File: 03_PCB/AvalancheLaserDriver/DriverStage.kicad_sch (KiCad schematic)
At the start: 20 parts

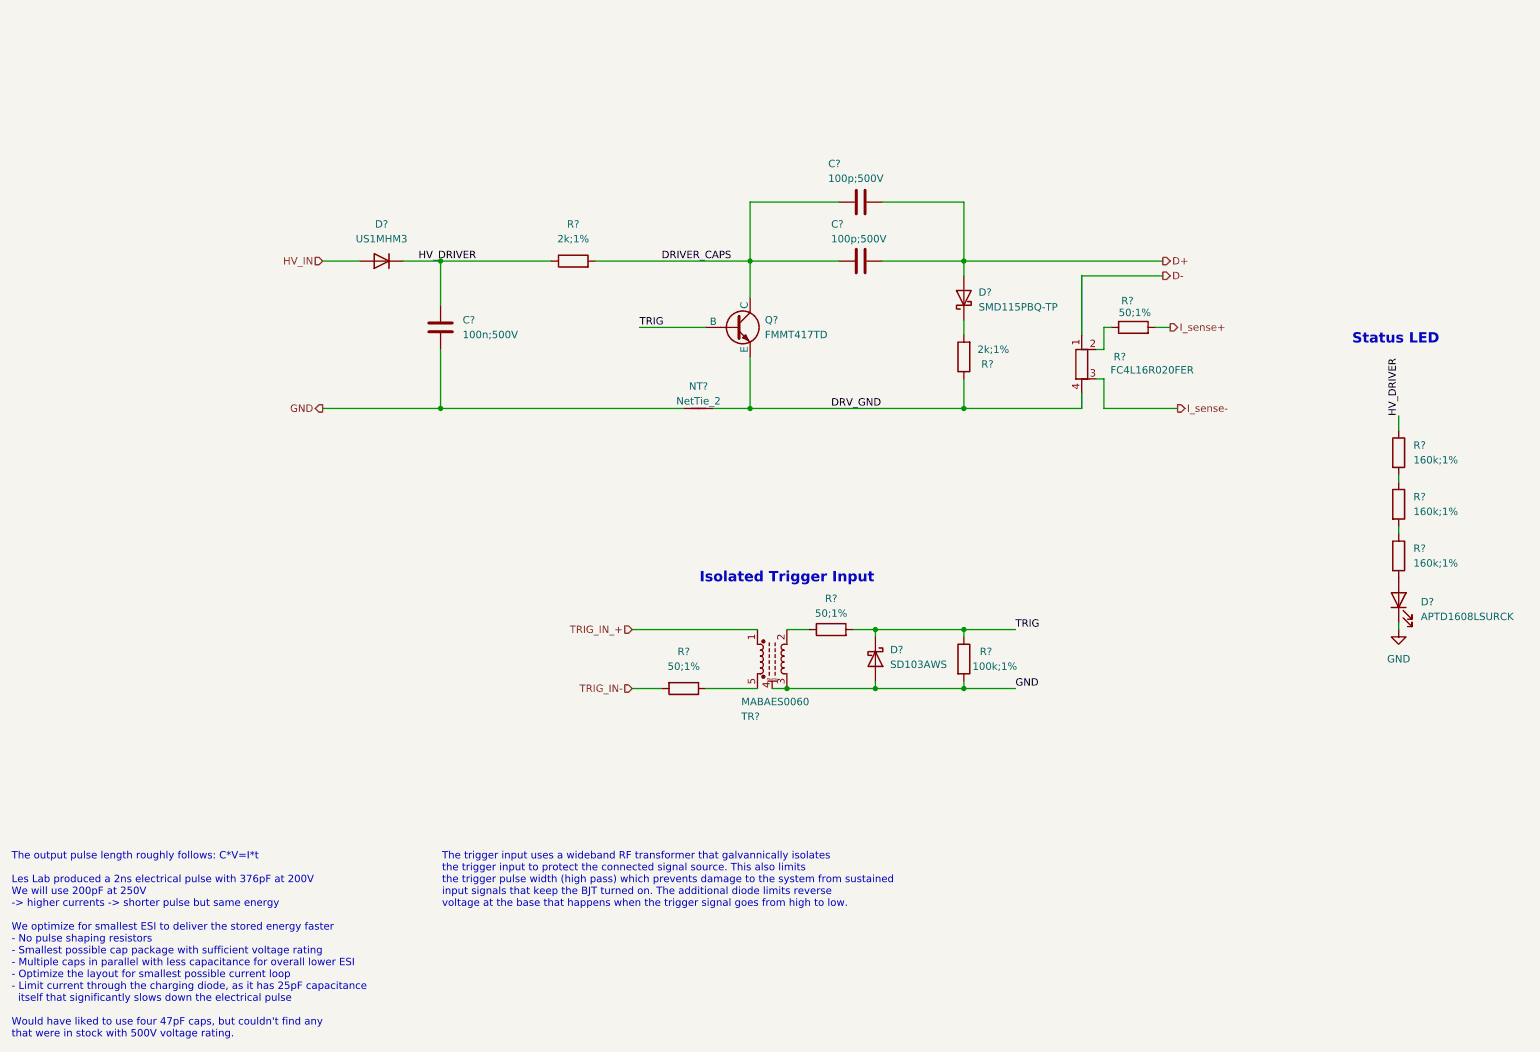
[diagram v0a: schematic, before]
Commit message: feat(pcb): edit component values after assembling first prototype
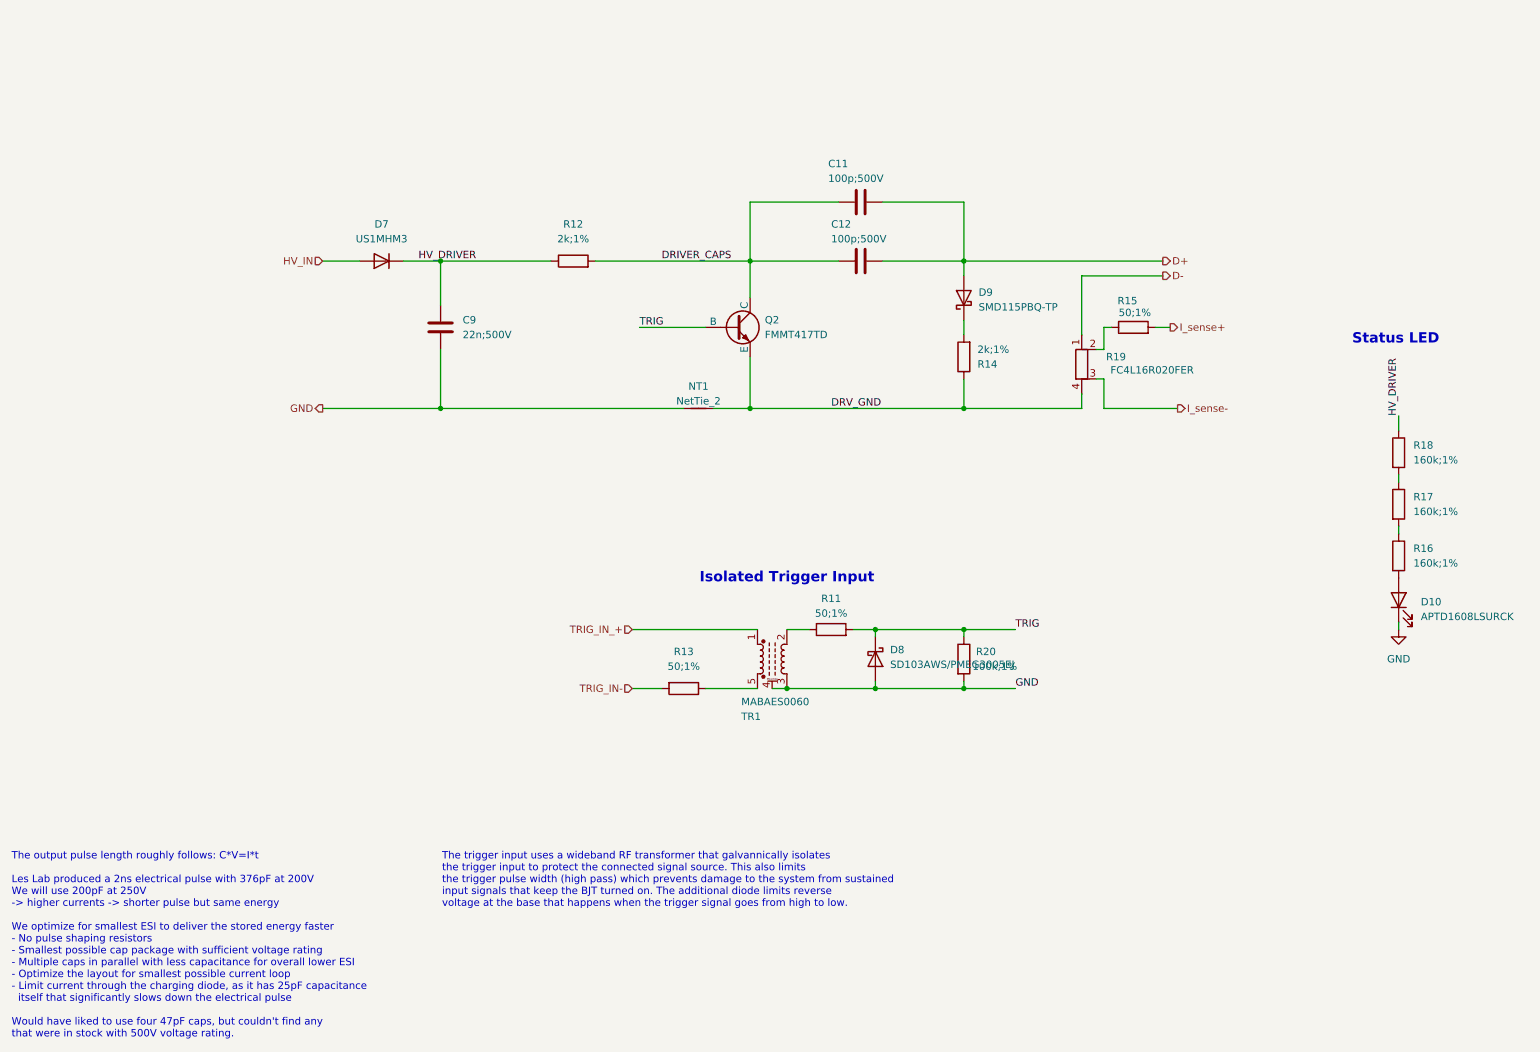
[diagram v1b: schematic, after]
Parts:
- C9: renamed from C?; value 100n;500V -> 22n;500V
- D8: renamed from D?; value SD103AWS -> SD103AWS/PMEG3005EJ
- gave numbers to parts that had none: 18
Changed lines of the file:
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@@
 		(dnp no)
 		(fields_autoplaced yes)
-		(property "Reference" "D?"
+		(property "Reference" "D7"
 			(at 78.74 57.15 0)
 			(effects
@@
 		(dnp no)
 		(fields_autoplaced yes)
-		(property "Reference" "R?"
+		(property "Reference" "R18"
 			(at 256.54 95.2499 0)
 			(effects
@@
 		(on_board yes)
 		(dnp no)
-		(property "Reference" "R?"
+		(property "Reference" "R20"
 			(at 182.88 130.81 0)
 			(effects
@@
 		(dnp no)
 		(fields_autoplaced yes)
-		(property "Reference" "D?"
+		(property "Reference" "D10"
 			(at 257.81 122.2374 90)
 			(effects
@@
 		(dnp no)
 		(fields_autoplaced yes)
-		(property "Reference" "#PWR?"
+		(property "Reference" "#PWR07"
 			(at 254 133.35 0)
 			(effects
@@
 		(dnp no)
 		(fields_autoplaced yes)
-		(property "Reference" "R?"
+		(property "Reference" "R16"
 			(at 256.54 113.0299 0)
 			(effects
@@
 		(dnp no)
 		(fields_autoplaced yes)
-		(property "Reference" "D?"
+		(property "Reference" "D9"
 			(at 181.61 68.8974 90)
 			(effects
@@
 		(on_board yes)
 		(dnp no)
-		(property "Reference" "TR?"
+		(property "Reference" "TR1"
 			(at 140.716 141.986 90)
 			(effects
@@
 		(on_board yes)
 		(dnp no)
-		(property "Reference" "R?"
+		(property "Reference" "R12"
 			(at 111.76 57.15 90)
 			(effects
@@
 		(dnp no)
 		(fields_autoplaced yes)
-		(property "Reference" "D?"
+		(property "Reference" "D8"
 			(at 166.37 130.4924 90)
 			(effects
@@
 			)
 		)
-		(property "Value" "SD103AWS"
+		(property "Value" "SD103AWS/PMEG3005EJ"
 			(at 166.37 133.0324 90)
 			(effects
@@
 		(on_board yes)
 		(dnp no)
-		(property "Reference" "C?"
+		(property "Reference" "C12"
 			(at 156.21 57.15 90)
 			(effects
@@
 		(on_board yes)
 		(dnp no)
-		(property "Reference" "NT?"
+		(property "Reference" "NT1"
 			(at 133.35 85.09 0)
 			(effects
@@
 		(dnp no)
 		(fields_autoplaced yes)
-		(property "Reference" "R?"
+		(property "Reference" "R17"
 			(at 256.54 104.1399 0)
 			(effects
@@
 		(on_board yes)
 		(dnp no)
-		(property "Reference" "R?"
+		(property "Reference" "R15"
 			(at 207.264 70.358 90)
 			(effects
@@
 		(dnp no)
 		(fields_autoplaced yes)
-		(property "Reference" "C?"
+		(property "Reference" "C9"
 			(at 92.71 73.6599 0)
 			(effects
@@
 			)
 		)
-		(property "Value" "100n;500V"
+		(property "Value" "22n;500V"
 			(at 92.71 76.1999 0)
 			(effects
@@
 		(on_board yes)
 		(dnp no)
-		(property "Reference" "R?"
+		(property "Reference" "R14"
 			(at 183.134 81.28 0)
 			(effects
@@
 		(on_board yes)
 		(dnp no)
-		(property "Reference" "Q?"
+		(property "Reference" "Q2"
 			(at 144.78 73.6599 0)
 			(effects
@@
 		(on_board yes)
 		(dnp no)
-		(property "Reference" "R?"
+		(property "Reference" "R11"
 			(at 156.21 121.666 90)
 			(effects
@@
 		(dnp no)
 		(fields_autoplaced yes)
-		(property "Reference" "R?"
+		(property "Reference" "R13"
 			(at 130.81 130.81 90)
 			(effects
@@
 		(on_board yes)
 		(dnp no)
-		(property "Reference" "R?"
+		(property "Reference" "R19"
 			(at 207.01 80.01 0)
 			(effects
@@
 		(on_board yes)
 		(dnp no)
-		(property "Reference" "C?"
+		(property "Reference" "C11"
 			(at 155.702 46.736 90)
 			(effects

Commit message: feat(pcb): update laser driver circuit after first iteration
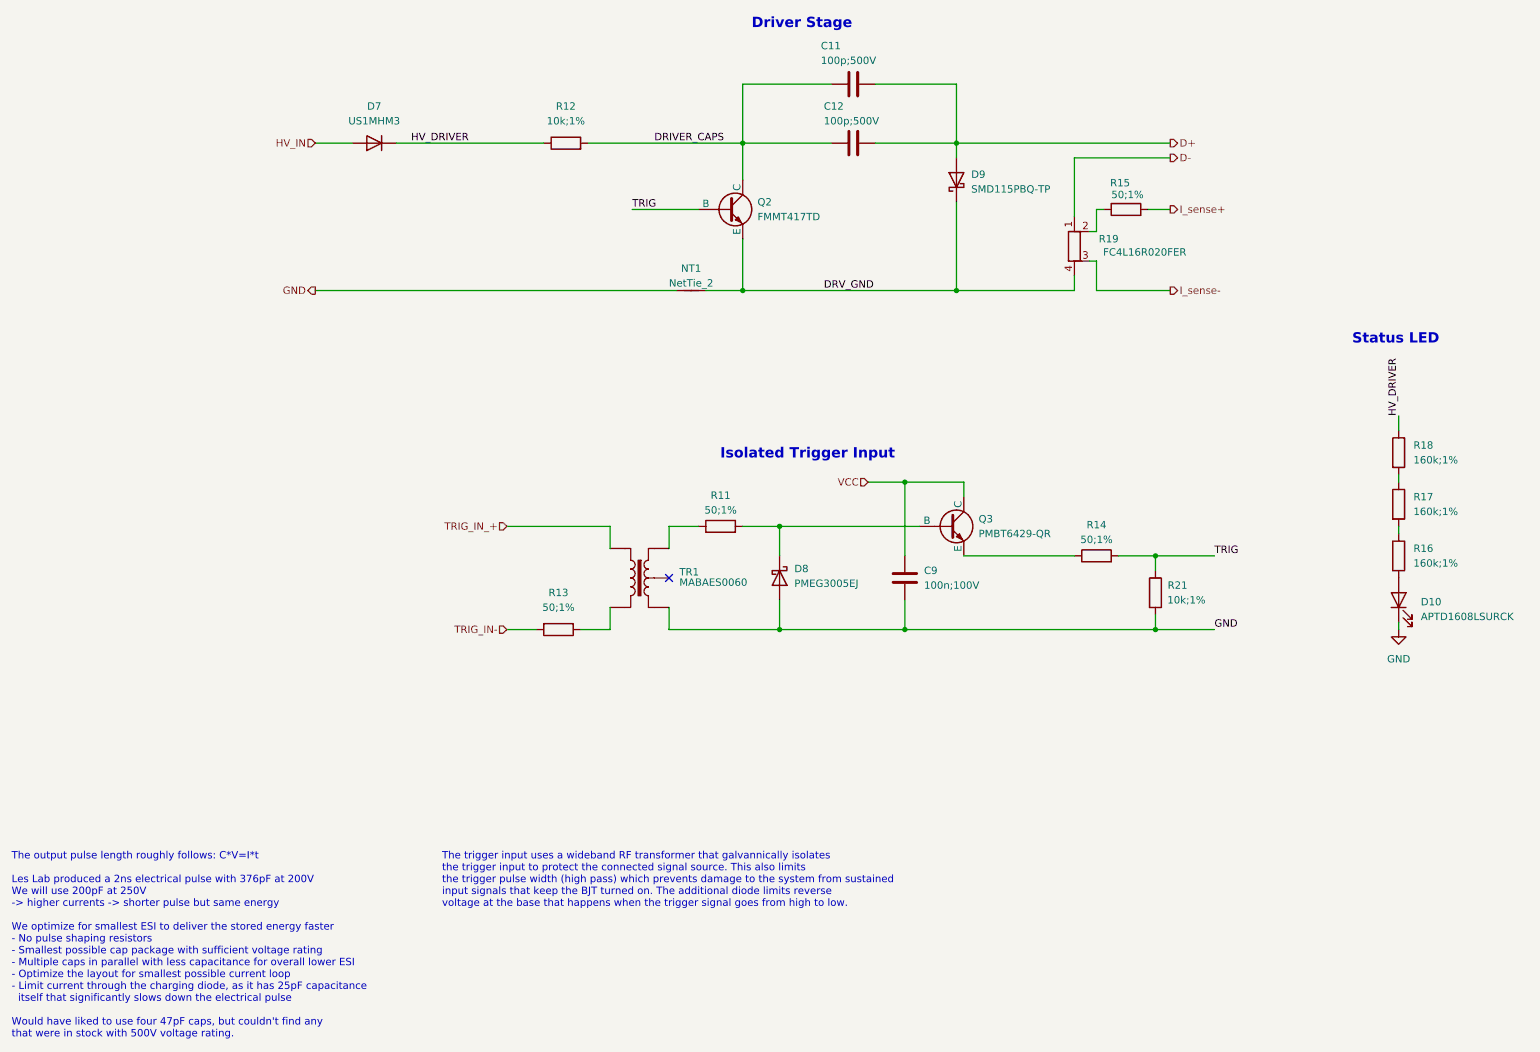
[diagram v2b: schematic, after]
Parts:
- removed R20: 100k;1%, Resistor_SMD:R_0603_1608Metric, symbol Device:R
- added Q3: PMBT6429-QR, Package_TO_SOT_SMD:TSOT-23, symbol Simulation_SPICE:NPN
- added R21: 10k;1%, Resistor_SMD:R_0603_1608Metric, symbol Device:R
- C9: value 22n;500V -> 100n;100V; footprint Capacitor_SMD:C_0805_2012Metric -> Capacitor_SMD:C_0603_1608Metric
- D8: value SD103AWS/PMEG3005EJ -> PMEG3005EJ; Alternatives Teil (none) -> SD103AWS
- R12: value 2k;1% -> 10k;1%; footprint Resistor_SMD:R_0805_2012Metric -> Resistor_SMD:R_0603_1608Metric
- R14: value 2k;1% -> 50;1%; footprint Resistor_SMD:R_0805_2012Metric -> Resistor_SMD:R_0603_1608Metric
- TR1: symbol Transformer:ETC1-1-13 -> Transformer:TRANSF4
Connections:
- net DRV_GND: now also D9.1 (K); no longer R14.1
- net GND: now also C9.1, TR1.5, R21.2; no longer C9.2, TR1.3, TR1.4 (MP)
- net HV_DRIVER: no longer C9.1
- net TRIG: now also R14.2, R21.1; no longer D8.1 (K), R11.2
- net TRIG_IN_+: now also TR1.2; no longer TR1.1
- net at R11.1: now also TR1.3; no longer TR1.2
- net at R13.1: now also TR1.1; no longer TR1.5
- new net: D8.1 (K), Q3.1 (B), R11.2
- new net: Q3.2 (E), R14.1
- new net VCC: C9.2, Q3.3 (C)
- no-connect marks 0 -> 1
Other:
- note added: "Driver Stage"
- moved on the sheet: C11, C12, D7, D8, D9, NT1, Q2, R11, R12, R13, R15, R19

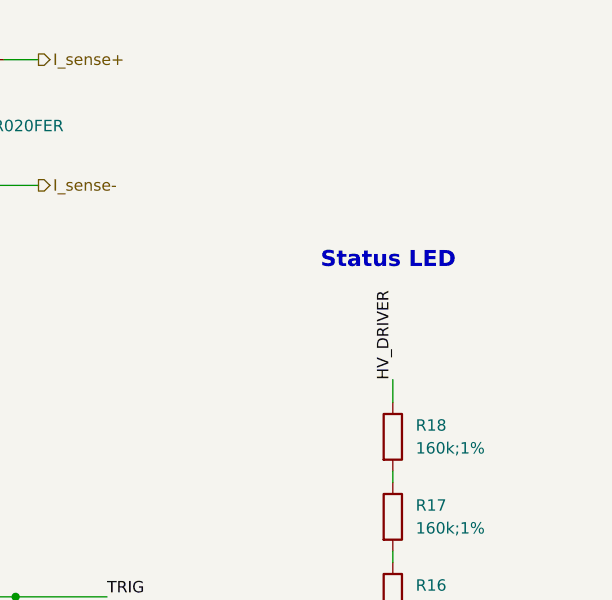
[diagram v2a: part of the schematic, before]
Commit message: feat(pcb): Increase operating voltage to 320V
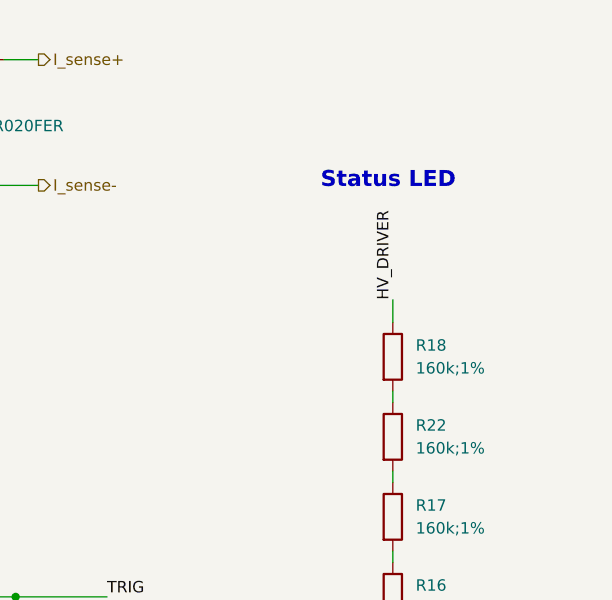
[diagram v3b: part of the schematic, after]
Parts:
- added R22: 160k;1%, Resistor_SMD:R_0603_1608Metric, symbol Device:R
- D7: footprint Diode_SMD:D_SOD-123 -> Diode_SMD:D_SOD-123F
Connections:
- net at R18.2: now also R22.1; no longer R17.1
- new net: R17.1, R22.2
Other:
- moved on the sheet: R18
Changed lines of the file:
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@@
 	(text "Status LED"
 		(exclude_from_sim no)
-		(at 253.492 76.962 0)
+		(at 253.492 68.072 0)
 		(effects
 			(font
@@
 	(wire
 		(pts
+			(xy 254 100.33) (xy 254 101.6)
+		)
+		(stroke
+			(width 0)
+			(type default)
+		)
+	)
+	(wire
+		(pts
 			(xy 198.12 45.72) (xy 214.63 45.72)
 		)
@@
 	(wire
 		(pts
-			(xy 254 90.17) (xy 254 92.71)
+			(xy 254 81.28) (xy 254 83.82)
 		)
 		(stroke
@@
 	(wire
 		(pts
-			(xy 254 100.33) (xy 254 101.6)
+			(xy 254 91.44) (xy 254 92.71)
 		)
 		(stroke
@@
 	)
 	(label "HV_DRIVER"
-		(at 254 90.17 90)
+		(at 254 81.28 90)
 		(effects
 			(font
@@
 			)
 		)
-		(property "Footprint" "Diode_SMD:D_SOD-123"
+		(property "Footprint" "Diode_SMD:D_SOD-123F"
 			(at 77.47 43.18 0)
 			(effects
@@
 	(symbol
 		(lib_id "Device:R")
-		(at 254 96.52 0)
+		(at 254 87.63 0)
 		(unit 1)
 		(exclude_from_sim no)
@@
 		(fields_autoplaced yes)
 		(property "Reference" "R18"
-			(at 256.54 95.2499 0)
+			(at 256.54 86.3599 0)
 			(effects
 				(font
@@
 		)
 		(property "Value" "160k;1%"
-			(at 256.54 97.7899 0)
+			(at 256.54 88.8999 0)
 			(effects
 				(font
@@
 		)
 		(property "Footprint" "Resistor_SMD:R_0603_1608Metric"
-			(at 252.222 96.52 90)
+			(at 252.222 87.63 90)
 			(effects
 				(font
@@
 		)
 		(property "Datasheet" "~"
-			(at 254 96.52 0)
+			(at 254 87.63 0)
 			(effects
 				(font
@@
 		)
 		(property "Description" "Resistor"
-			(at 254 96.52 0)
+			(at 254 87.63 0)
 			(effects
 				(font
@@
 					(unit 1)
 				)
+			)
+		)
+	)
+	(symbol
+		(lib_id "Device:R")
+		(at 254 96.52 0)
+		(unit 1)
+		(exclude_from_sim no)
+		(in_bom yes)
+		(on_board yes)
+		(dnp no)
+		(fields_autoplaced yes)
+		(property "Reference" "R22"
+			(at 256.54 95.2499 0)
+			(effects
+				(font
+					(size 1.27 1.27)
+				)
+				(justify left)
+			)
+		)
+		(property "Value" "160k;1%"
+			(at 256.54 97.7899 0)
+			(effects
+				(font
+					(size 1.27 1.27)
+				)
+				(justify left)
+			)
+		)
+		(property "Footprint" "Resistor_SMD:R_0603_1608Metric"
+			(at 252.222 96.52 90)
+			(effects
+				(font
+					(size 1.27 1.27)
+				)
+				(hide yes)
+			)
+		)
+		(property "Datasheet" "~"
+			(at 254 96.52 0)
+			(effects
+				(font
+					(size 1.27 1.27)
+				)
+				(hide yes)
+			)
+		)
+		(property "Description" "Resistor"
+			(at 254 96.52 0)
+			(effects
+				(font
+					(size 1.27 1.27)
+				)
+				(hide yes)
+			)
+		)
+		(pin "2"
+		)
+		(pin "1"
+		)
+		(instances
+			(project "AvalancheLaserDriver"
+				(path "/8e13b6ca-3b5b-4f2e-83bc-fdfde26a6699/c432be33-a0da-4a48-91d9-002ec1627f39"
+					(reference "R22")
+					(unit 1)
+				)

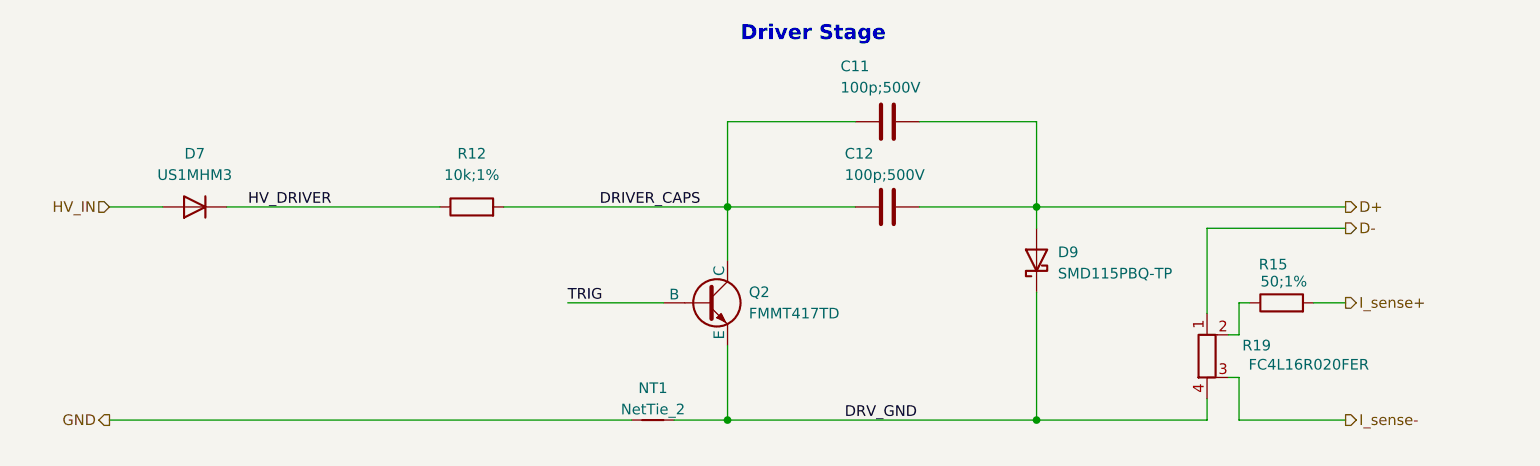
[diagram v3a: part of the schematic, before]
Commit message: feat(pcb): finalize layout of PCB V0.2
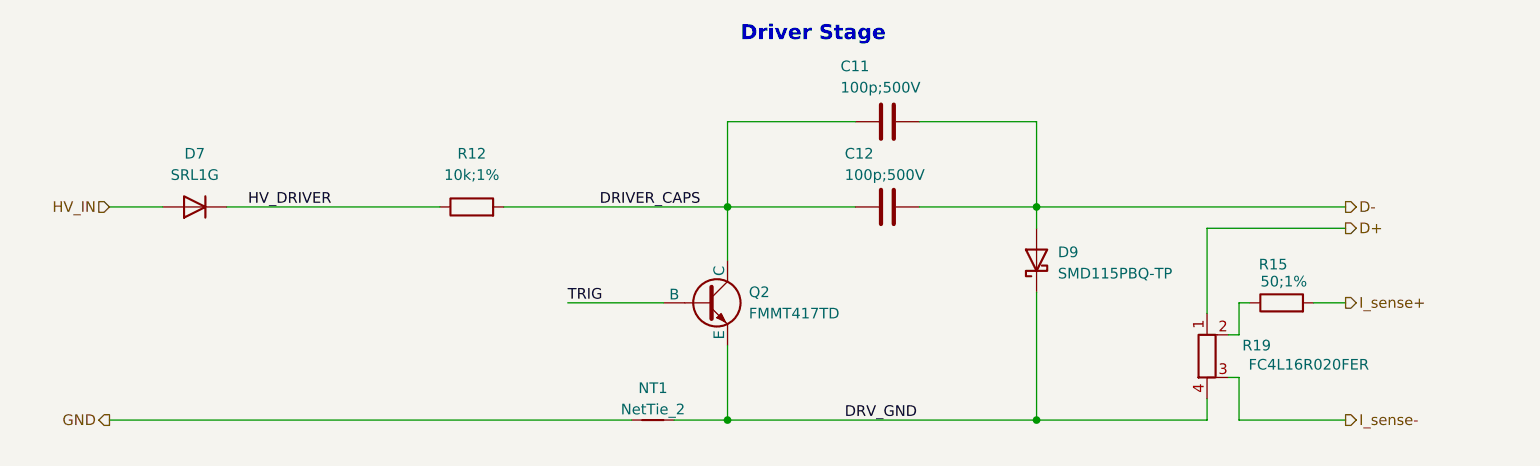
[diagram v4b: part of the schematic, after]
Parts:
- D7: value US1MHM3 -> SRL1G; footprint Diode_SMD:D_SOD-123F -> CustomFootprints:D_SOD-323HE
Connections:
- net D+: now also R19.1; no longer C11.2, C12.2, D9.2 (A)
- net D-: now also C11.2, C12.2, D9.2 (A); no longer R19.1
